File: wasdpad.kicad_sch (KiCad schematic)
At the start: 22 parts, among them SW1 SW_Push_45deg, SW2 SW_Push_45deg, SW3 SW_Push_45deg, SW4 SW_Push_45deg, SW5 SW_Push_45deg, SW6 SW_Push_45deg, U1 XIAO-RP2040-DIP

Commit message: pcb layout
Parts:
- SW1, SW2, SW3, SW4, SW5, SW6: footprint mx:MX-Hotswap-1U -> mx:MX-Solderable-1U
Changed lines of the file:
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@@
 			)
 		)
-		(property "Footprint" "mx:MX-Hotswap-1U"
+		(property "Footprint" "mx:MX-Solderable-1U"
 			(at 77.47 87.63 0)
 			(effects
@@
 			)
 		)
-		(property "Footprint" "mx:MX-Hotswap-1U"
+		(property "Footprint" "mx:MX-Solderable-1U"
 			(at 95.25 60.96 0)
 			(effects
@@
 			)
 		)
-		(property "Footprint" "mx:MX-Hotswap-1U"
+		(property "Footprint" "mx:MX-Solderable-1U"
 			(at 95.25 87.63 0)
 			(effects
@@
 			)
 		)
-		(property "Footprint" "mx:MX-Hotswap-1U"
+		(property "Footprint" "mx:MX-Solderable-1U"
 			(at 113.03 87.63 0)
 			(effects
@@
 			)
 		)
-		(property "Footprint" "mx:MX-Hotswap-1U"
+		(property "Footprint" "mx:MX-Solderable-1U"
 			(at 77.47 60.96 0)
 			(effects
@@
 			)
 		)
-		(property "Footprint" "mx:MX-Hotswap-1U"
+		(property "Footprint" "mx:MX-Solderable-1U"
 			(at 113.03 60.96 0)
 			(effects

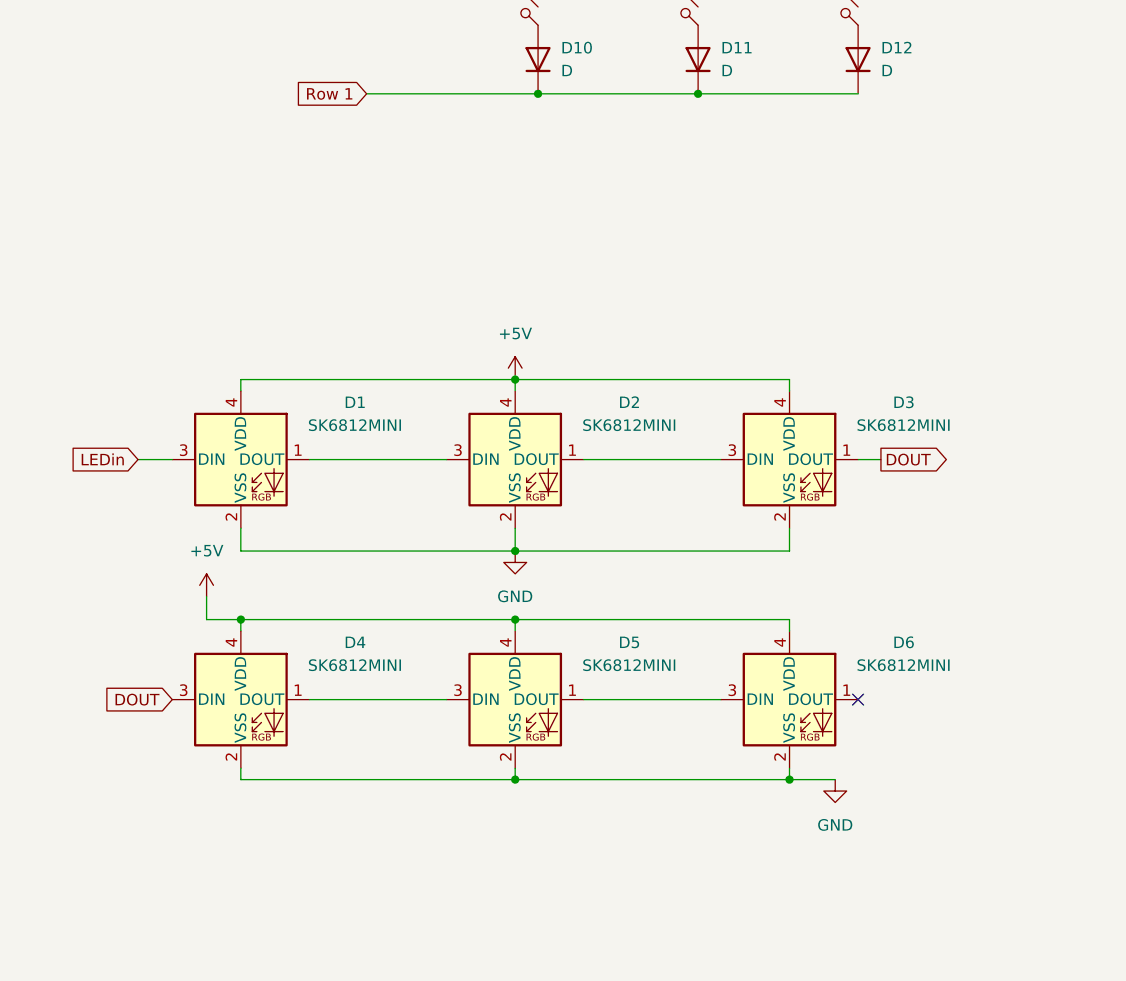
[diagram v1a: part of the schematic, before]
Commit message: extra neopixels
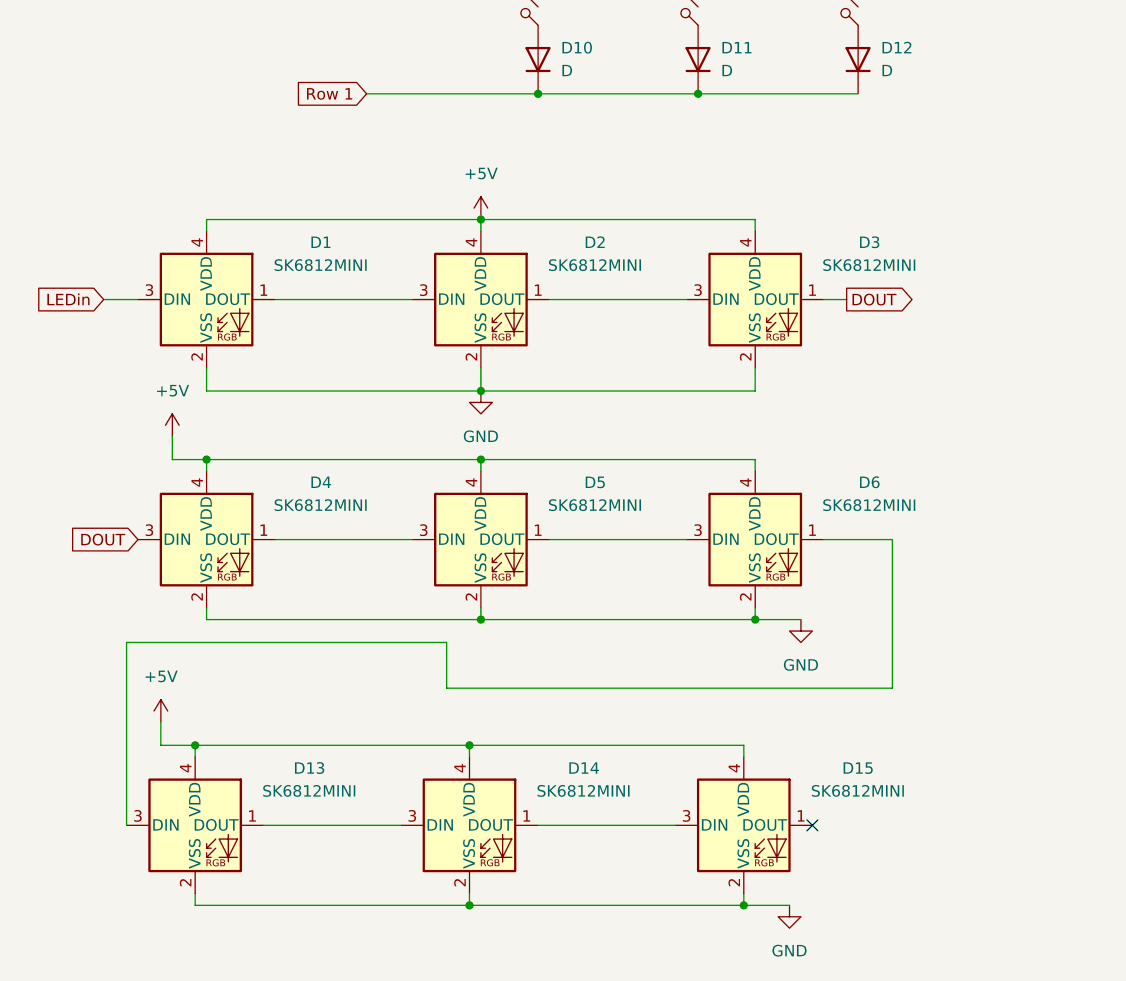
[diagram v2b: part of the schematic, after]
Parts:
- added D13, D14, D15: SK6812MINI, cyao:SK6812MINI-E, symbol LED:SK6812MINI
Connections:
- net +5V: now also D13.4 (VDD), D14.4 (VDD), D15.4 (VDD)
- net GND: now also D13.2 (VSS), D14.2 (VSS), D15.2 (VSS)
- net at D6.1 (DOUT): now also D13.3 (DIN)
- new net: D13.1 (DOUT), D14.3 (DIN)
- new net: D14.1 (DOUT), D15.3 (DIN)
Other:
- moved on the sheet: D1, D2, D3, D4, D5, D6

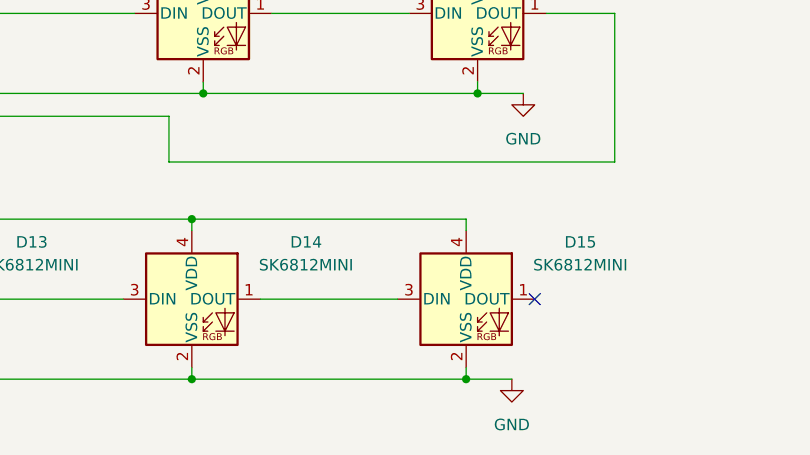
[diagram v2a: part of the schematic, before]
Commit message: add remaining 3d models
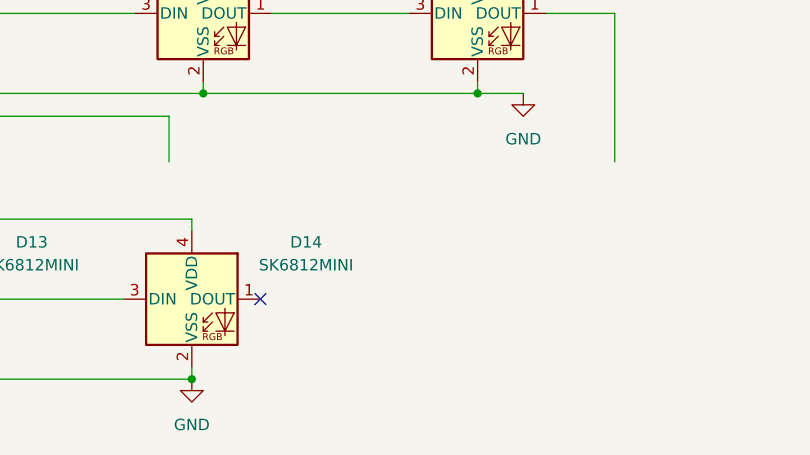
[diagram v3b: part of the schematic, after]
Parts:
- removed D15: SK6812MINI, cyao:SK6812MINI-E, symbol LED:SK6812MINI
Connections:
- net at D13.3 (DIN): no longer D6.1 (DOUT)
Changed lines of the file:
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@@
 	)
 	(junction
-		(at 72.39 170.18)
-		(diameter 0)
-		(color 0 0 0 0)
-	)
-	(junction
-		(at 102.87 187.96)
-		(diameter 0)
-		(color 0 0 0 0)
-	)
-	(junction
 		(at 73.66 130.81)
 		(diameter 0)
@@
 	)
 	(no_connect
-		(at 110.49 179.07)
+		(at 240.03 67.31)
 	)
 	(no_connect
-		(at 240.03 67.31)
+		(at 80.01 179.07)
 	)
 	(no_connect
@@
 	(wire
 		(pts
-			(xy 102.87 187.96) (xy 107.95 187.96)
-		)
-		(stroke
-			(width 0)
-			(type default)
-		)
-	)
-	(wire
-		(pts
 			(xy 73.66 111.76) (xy 73.66 113.03)
 		)
@@
 	(wire
 		(pts
-			(xy 72.39 170.18) (xy 102.87 170.18)
-		)
-		(stroke
-			(width 0)
-			(type default)
-		)
-	)
-	(wire
-		(pts
 			(xy 264.16 140.97) (xy 265.43 140.97)
 		)
@@
 	(wire
 		(pts
-			(xy 80.01 179.07) (xy 95.25 179.07)
-		)
-		(stroke
-			(width 0)
-			(type default)
-		)
-	)
-	(wire
-		(pts
 			(xy 80.01 97.79) (xy 97.79 97.79)
 		)
@@
 	(wire
 		(pts
-			(xy 102.87 170.18) (xy 102.87 171.45)
-		)
-		(stroke
-			(width 0)
-			(type default)
-		)
-	)
-	(wire
-		(pts
 			(xy 104.14 156.21) (xy 104.14 154.94)
 		)
@@
 	(wire
 		(pts
-			(xy 119.38 163.83) (xy 69.85 163.83)
-		)
-		(stroke
-			(width 0)
-			(type default)
-		)
-	)
-	(wire
-		(pts
 			(xy 92.71 41.91) (xy 92.71 58.42)
 		)
@@
 	(wire
 		(pts
-			(xy 72.39 187.96) (xy 102.87 187.96)
-		)
-		(stroke
-			(width 0)
-			(type default)
-		)
-	)
-	(wire
-		(pts
 			(xy 97.79 97.79) (xy 115.57 97.79)
 		)
@@
 	(wire
 		(pts
-			(xy 102.87 187.96) (xy 102.87 186.69)
-		)
-		(stroke
-			(width 0)
-			(type default)
-		)
-	)
-	(wire
-		(pts
 			(xy 119.38 147.32) (xy 119.38 163.83)
 		)
@@
 	(symbol
 		(lib_id "LED:SK6812MINI")
-		(at 102.87 179.07 0)
-		(unit 1)
-		(exclude_from_sim no)
-		(in_bom yes)
-		(on_board yes)
-		(dnp no)
-		(fields_autoplaced yes)
-		(property "Reference" "D15"
-			(at 115.57 172.7514 0)
-			(effects
-				(font
-					(size 1.27 1.27)
-				)
-			)
-		)
-		(property "Value" "SK6812MINI"
-			(at 115.57 175.2914 0)
-			(effects
-				(font
-					(size 1.27 1.27)
-				)
-			)
-		)
-		(property "Footprint" "cyao:SK6812MINI-E"
-			(at 104.14 186.69 0)
-			(effects
-				(font
-					(size 1.27 1.27)
-				)
-				(justify left top)
-				(hide yes)
-			)
-		)
-		(property "Datasheet" "https://cdn-shop.adafruit.com/product-files/2686/SK6812MINI_REV.01-1-2.pdf"
-			(at 105.41 188.595 0)
-			(effects
-				(font
-					(size 1.27 1.27)
-				)
-				(justify left top)
-				(hide yes)
-			)
-		)
-		(property "Description" "RGB LED with integrated controller"
-			(at 102.87 179.07 0)
-			(effects
-				(font
-					(size 1.27 1.27)
-				)
-				(hide yes)
-			)
-		)
-		(pin "1"
-		)
-		(pin "4"
-		)
-		(pin "3"
-		)
-		(pin "2"
-		)
-		(instances
-			(project "wasdpad"
-				(path "/805b6d72-f66d-4982-bf60-6dd7fd1c889a"
-					(reference "D15")
-					(unit 1)
-				)
-			)
-		)
-	)
-	(symbol
-		(lib_id "LED:SK6812MINI")
 		(at 43.18 120.65 0)
 		(unit 1)
@@
 	(symbol
 		(lib_id "power:GND")
-		(at 107.95 187.96 0)
+		(at 72.39 187.96 0)
 		(unit 1)
 		(exclude_from_sim no)
@@
 		(fields_autoplaced yes)
 		(property "Reference" "#PWR012"
-			(at 107.95 194.31 0)
+			(at 72.39 194.31 0)
 			(effects
 				(font
@@
 		)
 		(property "Value" "GND"
-			(at 107.95 193.04 0)
+			(at 72.39 193.04 0)
 			(effects
 				(font
@@
 		)
 		(property "Footprint" ""
-			(at 107.95 187.96 0)
+			(at 72.39 187.96 0)
 			(effects
 				(font
@@
 		)
 		(property "Datasheet" ""
-			(at 107.95 187.96 0)
+			(at 72.39 187.96 0)
 			(effects
 				(font
@@
 		)
 		(property "Description" "Power symbol creates a global label with name \"GND\" , ground"
-			(at 107.95 187.96 0)
+			(at 72.39 187.96 0)
 			(effects
 				(font
